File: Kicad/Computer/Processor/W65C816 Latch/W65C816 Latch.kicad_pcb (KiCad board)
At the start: 2 copper layers, 26.7 x 24.1 mm, 13 parts, among them IC1 74LVC08APW,112, J1 Pin_Header_01x06, J2 Conn_02x06_Counter_Clockwise, J3 Pin_Header_01x06

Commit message: Tidied and re-routed the Video Boards
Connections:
- net /Bank Latch renamed Bank Latch
- net /~{PHI2} renamed ~{PHI2}
- net /~{Trans Out} renamed ~{Trans Out}
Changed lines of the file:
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@@
 	(net 3 "/~{PHI2}_{2}")
 	(net 4 "/~{PHI2}_{3}")
-	(net 5 "/Bank Latch")
-	(net 6 "/~{Trans Out}")
+	(net 5 "Bank Latch")
+	(net 6 "~{Trans Out}")
 	(net 7 "Net-(IC1-3Y)")
-	(net 8 "/~{PHI2}")
+	(net 8 "~{PHI2}")
 	(net 9 "Net-(IC1-4Y)")
 	(net 10 "Net-(IC1-2Y)")
@@
 			(layers "F.Cu" "F.Paste" "F.Mask")
 			(roundrect_rratio 0.243902)
-			(net 6 "/~{Trans Out}")
+			(net 6 "~{Trans Out}")
 			(pintype "passive")
 		)
@@
 			(layers "F.Cu" "F.Paste" "F.Mask")
 			(roundrect_rratio 0.25)
-			(net 6 "/~{Trans Out}")
+			(net 6 "~{Trans Out}")
 			(pintype "passive")
 		)
@@
 			(size 0.45 1.475)
 			(layers "F.Cu" "F.Paste" "F.Mask")
-			(net 8 "/~{PHI2}")
+			(net 8 "~{PHI2}")
 			(pinfunction "1A")
 			(pintype "input")
@@
 			(size 0.45 1.475)
 			(layers "F.Cu" "F.Paste" "F.Mask")
-			(net 8 "/~{PHI2}")
+			(net 8 "~{PHI2}")
 			(pinfunction "1B")
 			(pintype "input")
@@
 			(size 0.45 1.475)
 			(layers "F.Cu" "F.Paste" "F.Mask")
-			(net 8 "/~{PHI2}")
+			(net 8 "~{PHI2}")
 			(pinfunction "3A")
 			(pintype "input")
@@
 			(layers "F.Cu" "F.Paste" "F.Mask")
 			(roundrect_rratio 0.243902)
-			(net 5 "/Bank Latch")
+			(net 5 "Bank Latch")
 			(pintype "passive")
 		)
@@
 			(layers "F.Cu" "F.Paste" "F.Mask")
 			(roundrect_rratio 0.25)
-			(net 5 "/Bank Latch")
+			(net 5 "Bank Latch")
 			(pintype "passive")
 		)
@@
 			(layers "*.Cu" "*.Mask")
 			(remove_unused_layers no)
-			(net 8 "/~{PHI2}")
+			(net 8 "~{PHI2}")
 			(pinfunction "Pin_3")
 			(pintype "passive")
@@
 			(layers "*.Cu" "*.Mask")
 			(remove_unused_layers no)
-			(net 6 "/~{Trans Out}")
+			(net 6 "~{Trans Out}")
 			(pinfunction "Pin_9")
 			(pintype "passive")
@@
 			(layers "*.Cu" "*.Mask")
 			(remove_unused_layers no)
-			(net 5 "/Bank Latch")
+			(net 5 "Bank Latch")
 			(pinfunction "Pin_10")
 			(pintype "passive")

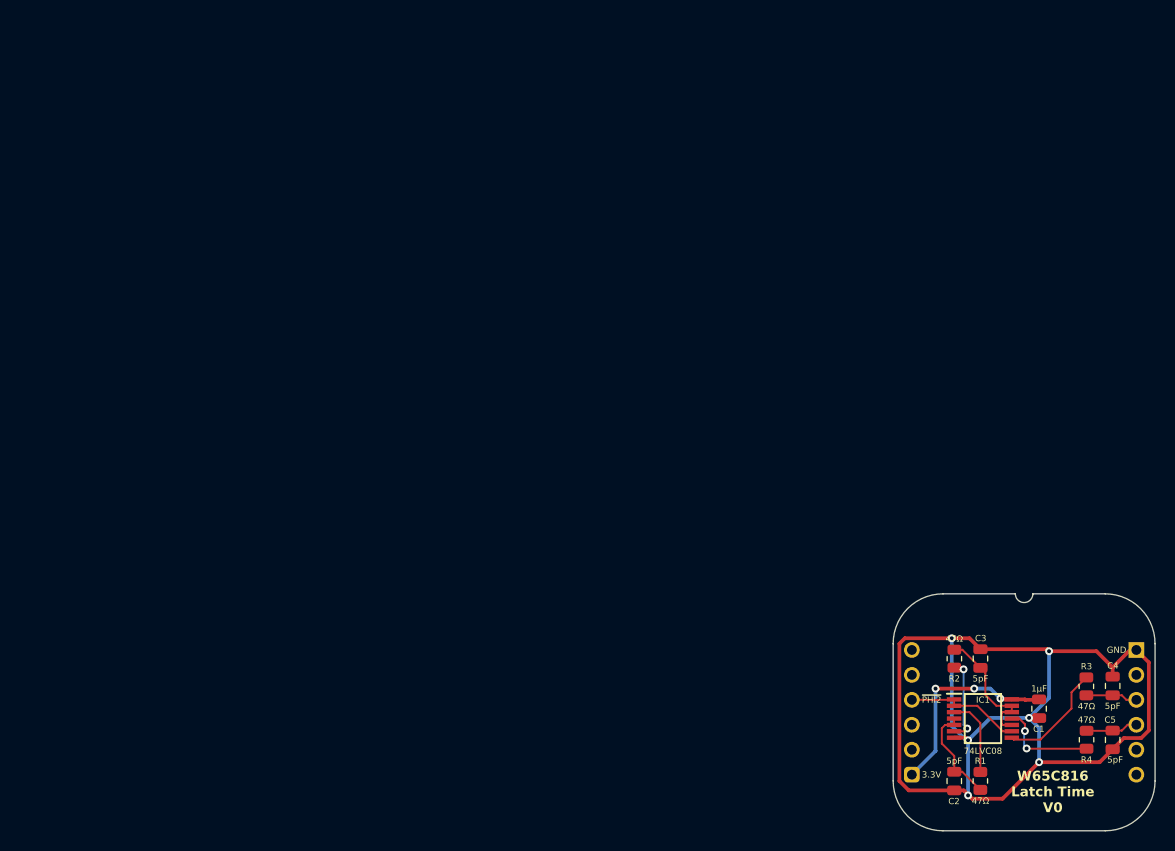
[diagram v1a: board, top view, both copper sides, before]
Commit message: Use VRML instead of STEPs for Processor Board models.
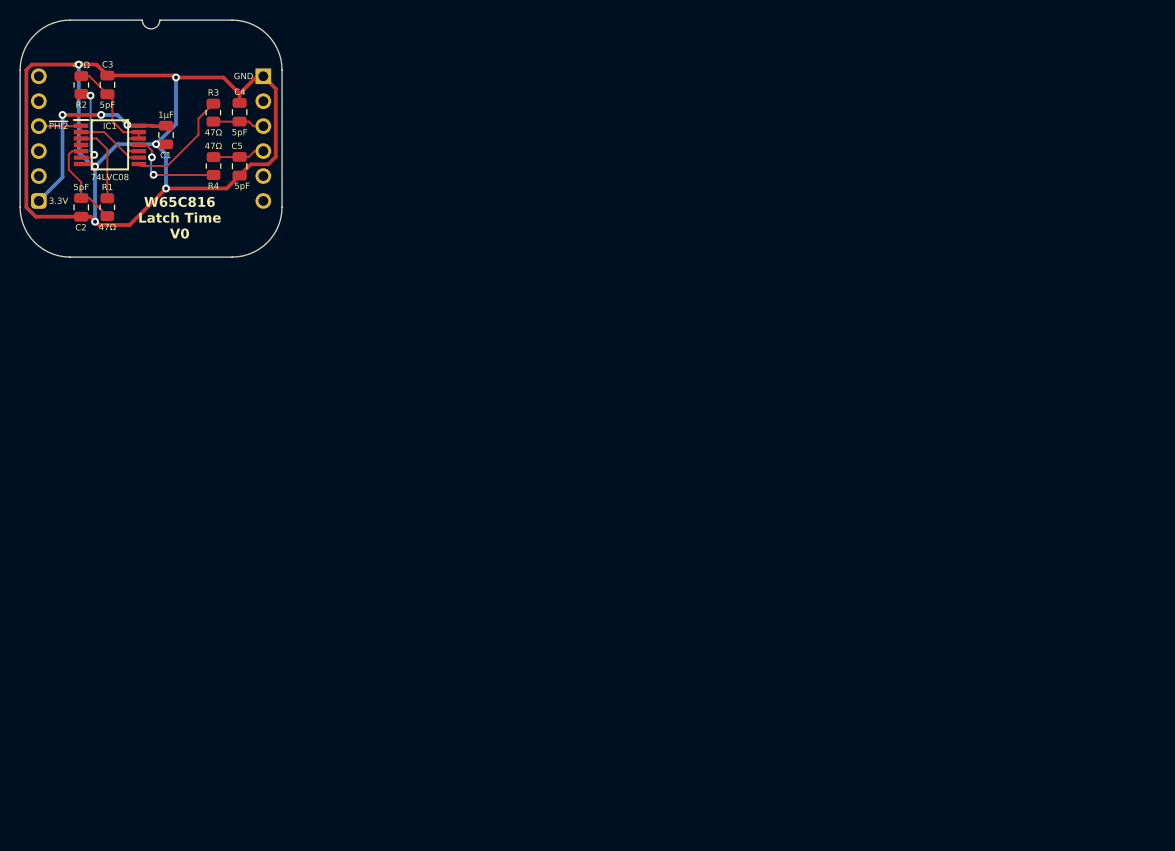
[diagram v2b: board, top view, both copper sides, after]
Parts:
- moved C1 106.4 mm to (13.0, 5.97)
- moved C2 106.4 mm to (4.32, 13.3)
- moved C3 106.4 mm to (6.99, 0.89)
- moved J1 106.4 mm to (22.9, 0.00)
- moved J2 106.4 mm to (0.00, 0.00)
- moved J3 106.4 mm to (0.00, 0.00)
- moved R1 106.4 mm to (6.99, 13.3)
- moved R2 106.4 mm to (4.32, 0.89)
- moved R3 106.4 mm to (17.8, 3.71)
- moved R4 106.4 mm to (17.8, 9.14)
- moved C4 106.4 mm to (20.4, 3.68)
- moved C5 106.4 mm to (20.4, 9.14)
- moved IC1 106.4 mm to (7.24, 6.99)
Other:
- outline, holes or cut-outs redrawn

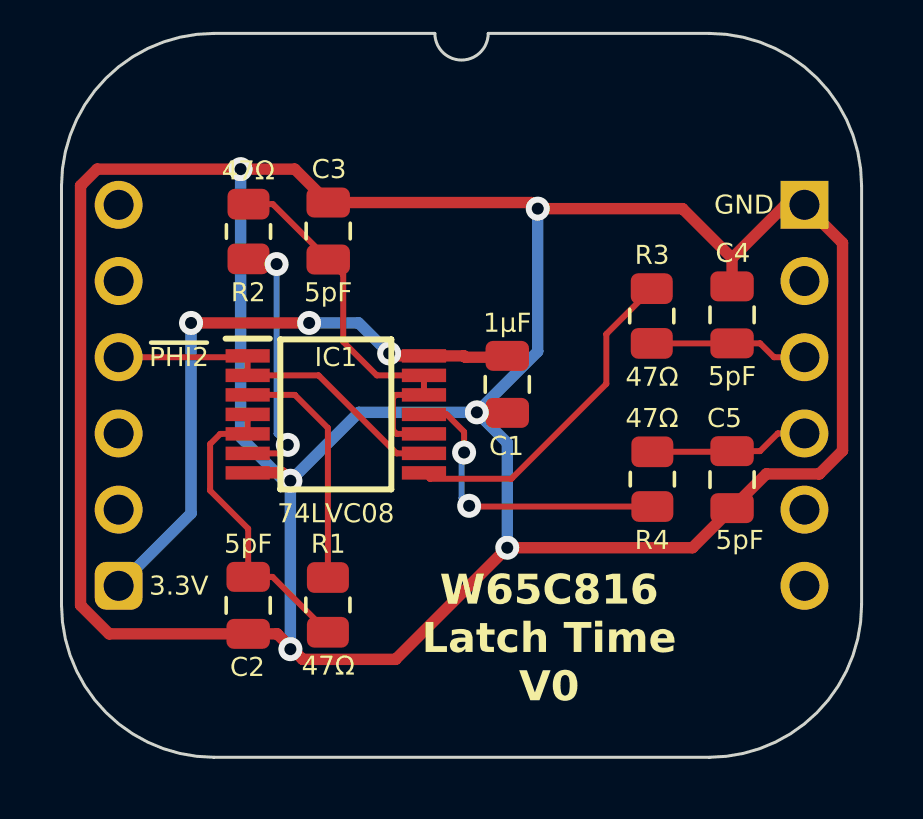
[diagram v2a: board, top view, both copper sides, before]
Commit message: Renamed Trans Out to Data Output.
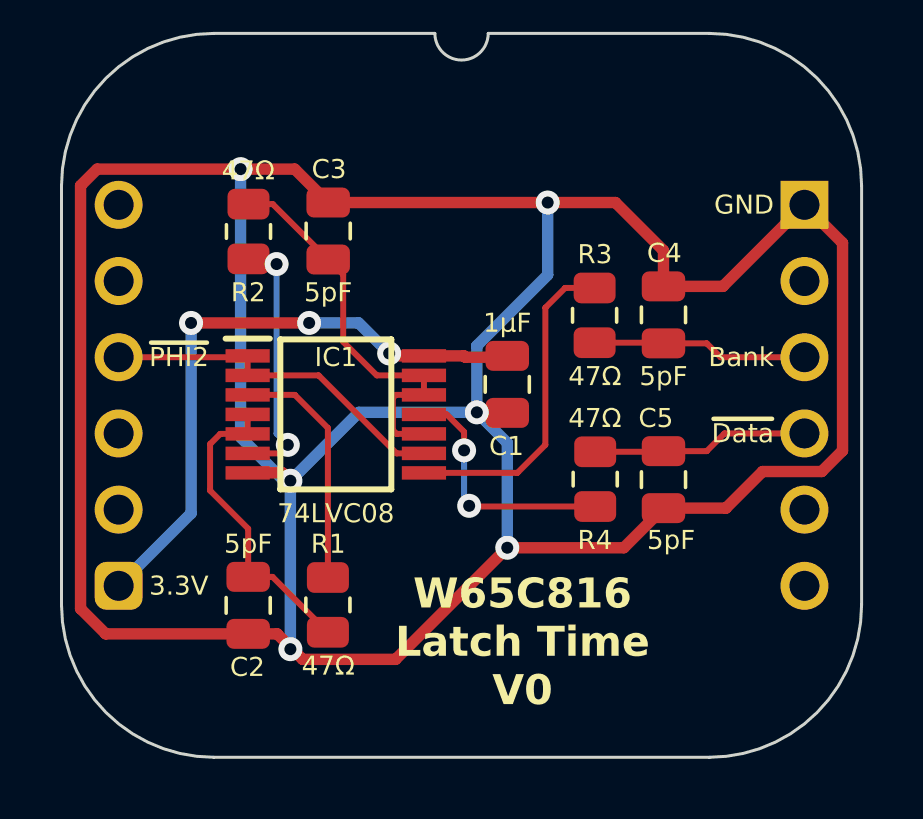
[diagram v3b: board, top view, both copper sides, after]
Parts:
- moved C4 2.29 mm to (18.2, 3.68)
- moved C5 2.29 mm to (18.2, 9.14)
- moved R3 1.91 mm to (15.9, 3.68)
- moved R4 1.91 mm to (15.9, 9.14)
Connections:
- net ~{Trans Out} renamed ~{Data Output}
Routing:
- net Bank Latch: track 5.28 -> 7.61 mm
- net Net-(IC1-4Y): track 10.3 -> 8.33 mm
- net ~{Data Output}: track 5.29 -> 7.23 mm
- net GND: track 118.1 -> 119.0 mm
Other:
- board text added: "Bank"
- board text added: "~{Data}"

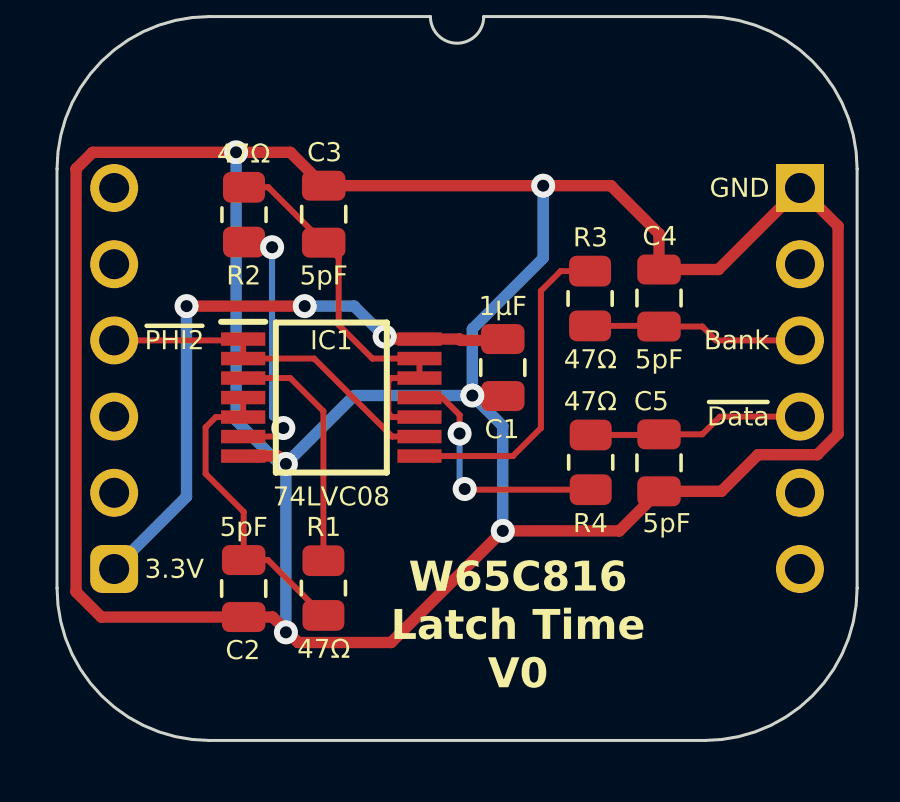
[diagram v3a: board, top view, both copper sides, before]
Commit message: Rounded Clock Hold traces.
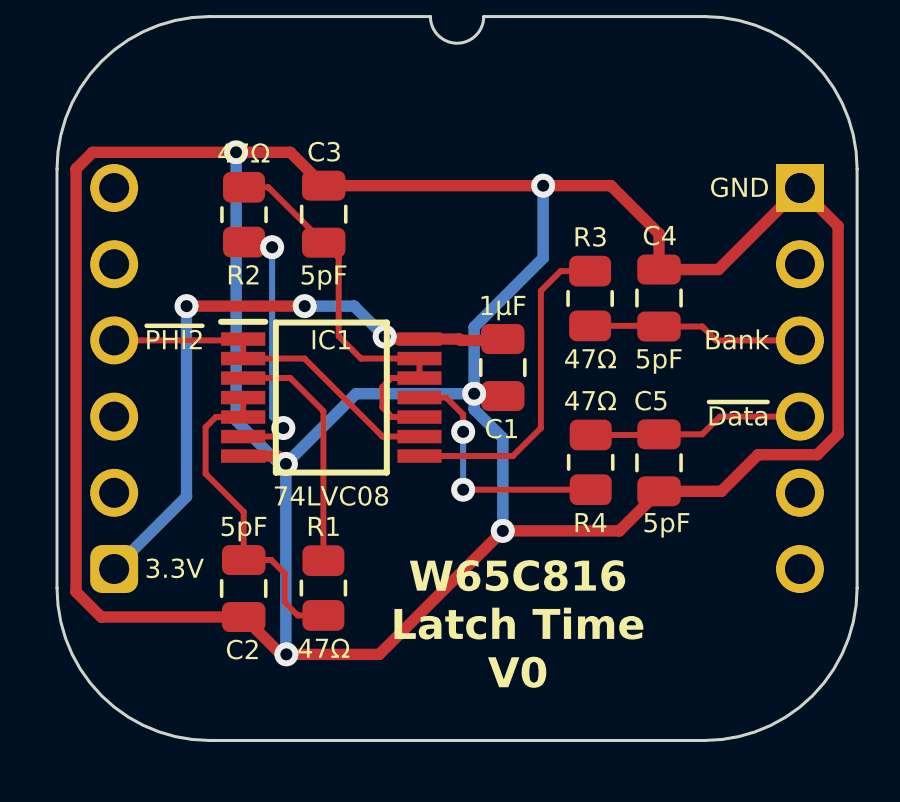
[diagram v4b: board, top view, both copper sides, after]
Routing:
- net GND: track 119.0 -> 120.1 mm
- net /~{PHI2}_{2}: track 10.4 -> 11.0 mm

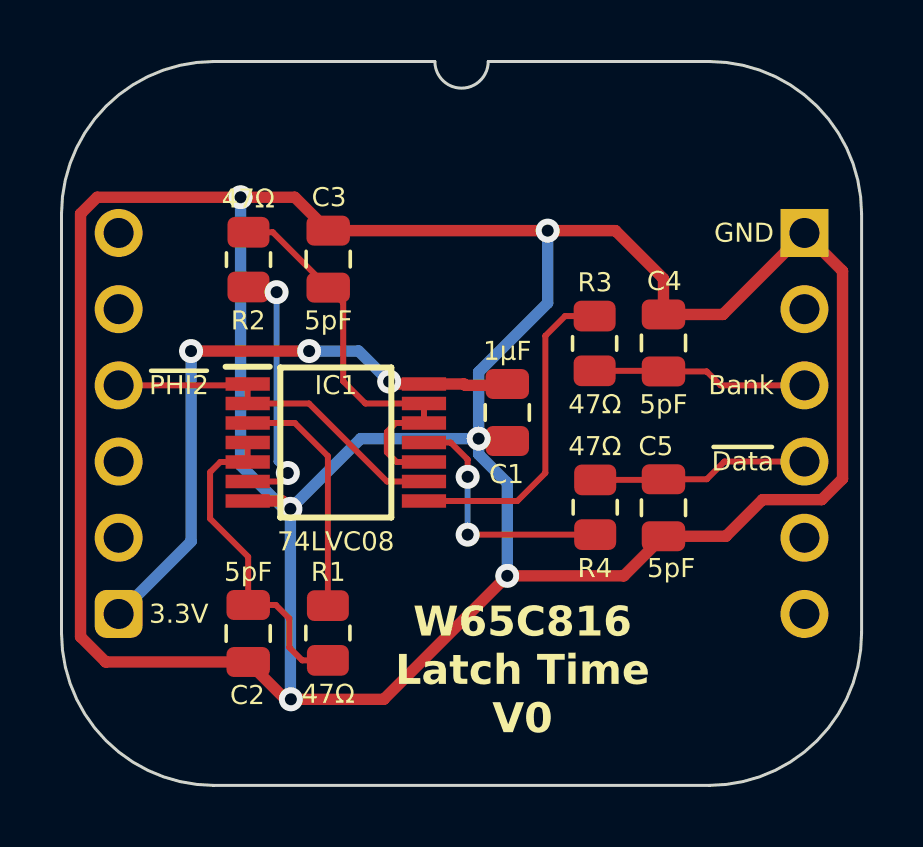
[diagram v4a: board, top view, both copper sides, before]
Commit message: Added Coprocessor Board and shrunk W65C816 Latch.
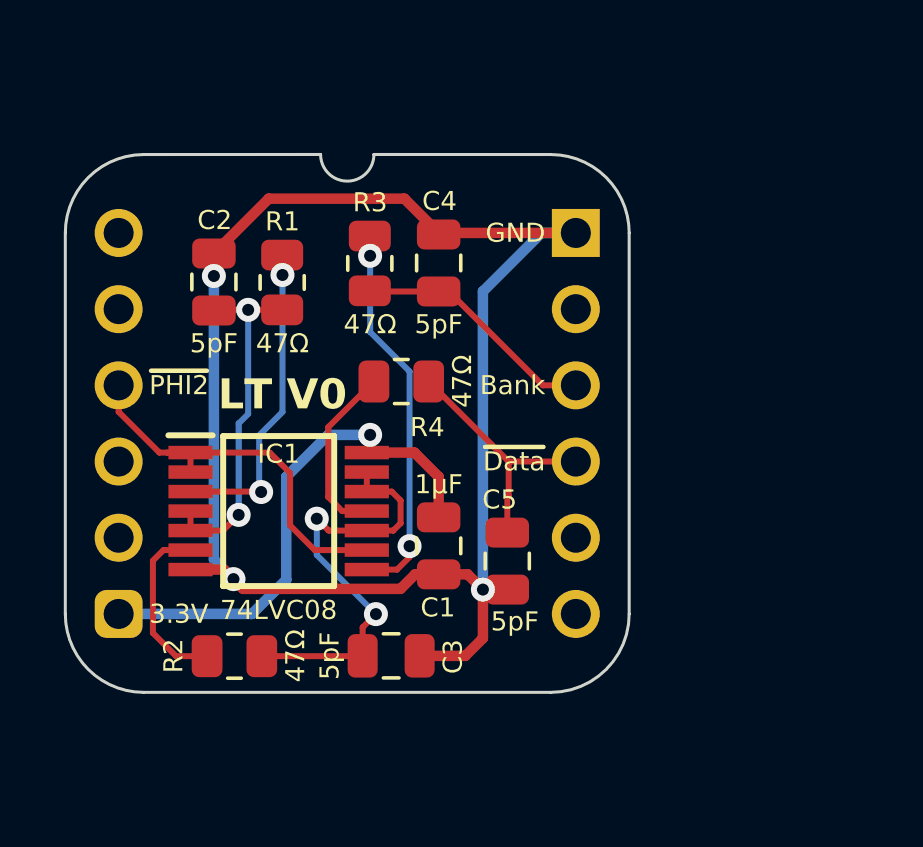
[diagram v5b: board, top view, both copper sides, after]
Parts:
- J2: footprint SamacSys_Parts:DIP-12_Board_W22.86mm_Alt -> SamacSys_Parts:DIP-12_Board_W15.24mm_Alt
- moved C3 13.4 mm to (9.07, 14.1), turned to -90 degrees
- moved R2 13.2 mm to (3.86, 14.1), turned to 90 degrees
- moved R1 11.8 mm to (5.46, 1.65)
- moved C2 11.7 mm to (3.17, 1.65), turned to 0 degrees
- moved C4 7.95 mm to (10.7, 1.02)
- moved R3 7.95 mm to (8.38, 1.02)
- moved R4 7.70 mm to (9.42, 4.94), turned to 90 degrees
- moved J1 7.62 mm to (15.2, 0.00)
- moved C5 5.50 mm to (13.0, 10.9)
- moved C1 5.00 mm to (10.7, 10.4)
- moved IC1 2.98 mm to (5.33, 9.27)
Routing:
- net GND: track 120.1 -> 53.0 mm, vias 6 -> 3
- net 3.3V: track 20.7 -> 17.4 mm, vias 3 -> 1
- net Net-(IC1-2Y): track 8.65 -> 5.94 mm, vias 2 -> 0
- net Net-(IC1-1Y): track 8.12 -> 10.6 mm, vias 0 -> 2
- net Net-(IC1-4Y): track 8.45 -> 5.96 mm, vias 2 -> 0
- net Net-(IC1-3Y): track 10.9 -> 12.8 mm, vias 0 -> 2
- net ~{Data Output}: track 7.20 -> 8.40 mm
- net /~{PHI2}_{3}: track 13.8 -> 14.6 mm, vias 0 -> 2
- net /~{PHI2}_{2}: track 11.0 -> 11.7 mm, vias 0 -> 2
- net Bank Latch: track 7.17 -> 7.80 mm
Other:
- board size 26.7 x 24.1 mm -> 18.8 x 17.9 mm
- board text added: "LT V0"
- board text removed: "W65C816 Latch Time V0"

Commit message: Processor boards with proper board schematic symbol and global labels.
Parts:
- removed J1, J3: Pin_Header_01x06, SamacSys_Parts:PinHeader_1x06_P2.54mm_Vertical
- J2: value Conn_02x06_Counter_Clockwise -> Board 2x06 W15.24mm
